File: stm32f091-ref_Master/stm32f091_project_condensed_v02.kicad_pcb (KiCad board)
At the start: 4 copper layers, 68 parts, among them J1 Conn_02x05_Odd_Even, J2 Conn_01x09_Female, J3 Conn_01x08_Female, J4 Conn_01x02_Female, SW1 SW_Push, SW2 SW_Push, U1 LD1117S33TR_SOT223, U2 LM324, U3 STM32F091RCTx, U4 LM386

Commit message: new pcb design
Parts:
- moved J1 0.30 mm to (134.1, 87.9)
- moved R21 0.23 mm to (127.0, 109.2)
- moved J2 0.09 mm to (140.8, 122.8)
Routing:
- net GND: track 10.5 -> 164.3 mm, vias 0 -> 20
- net 3.3V: track 73.1 -> 218.0 mm, vias 0 -> 16
- net /PA13: track 94.0 -> 50.2 mm, vias 0 -> 4
- net /PA4: track 0.00 -> 28.8 mm, vias 0 -> 2
- net Net-(C18-Pad1): track 38.3 -> 64.3 mm, vias 0 -> 1
- net PB8: track 38.0 -> 16.7 mm, vias 0 -> 1
- net PB14: track 17.6 -> 33.8 mm, vias 0 -> 1
- net /PB2: track 2.30 -> 17.0 mm, vias 0 -> 2
- net /NRST: track 36.7 -> 48.0 mm, vias 0 -> 2
- net 5.5V: track 177.1 -> 186.1 mm
- net /PA14: track 72.3 -> 66.7 mm
- net /PC7: track 25.7 -> 31.0 mm
- net Net-(C18-Pad2): track 47.0 -> 50.3 mm, vias 0 -> 1
- net /PC6: track 30.6 -> 33.8 mm, vias 0 -> 4
- net /U5V: track 0.00 -> 2.54 mm
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- added copper zone on B.Cu, net GND
- added copper zone on F.Cu, net GND

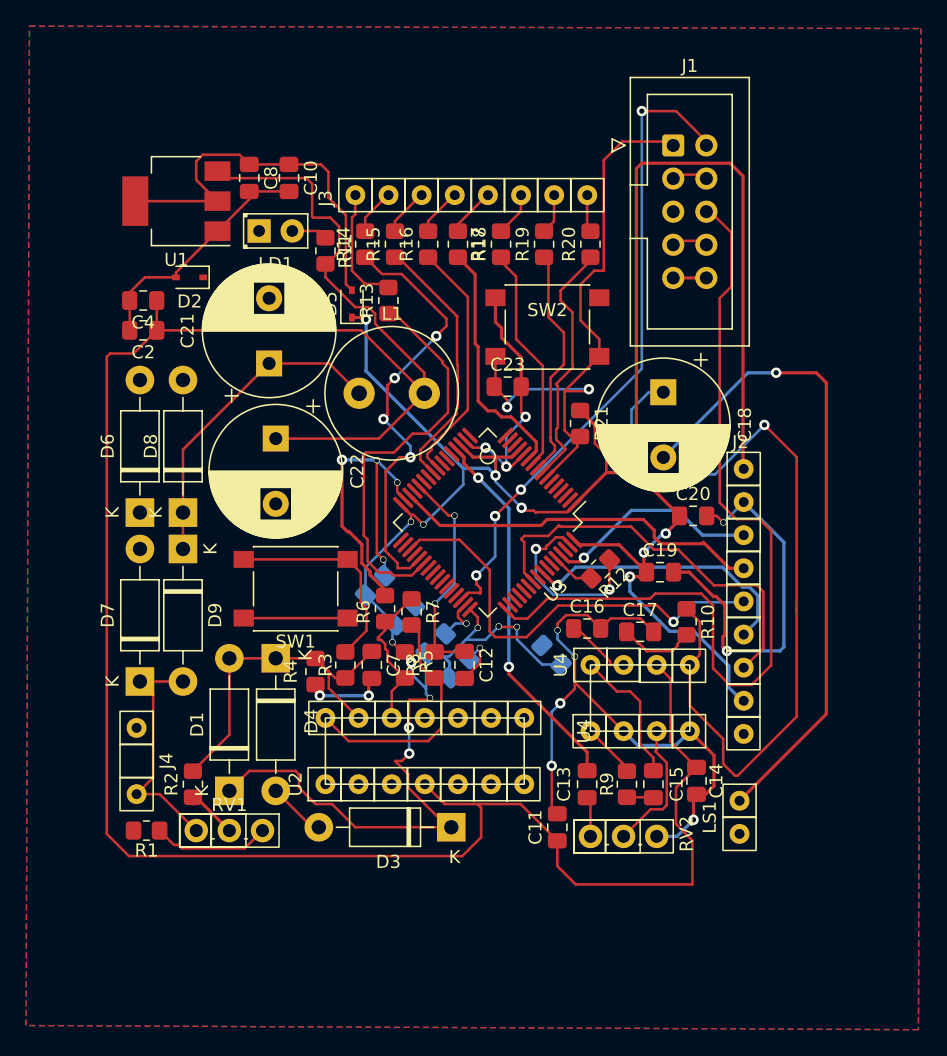
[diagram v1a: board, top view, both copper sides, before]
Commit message: minor tracing changes and edge cut added for v02 pcb
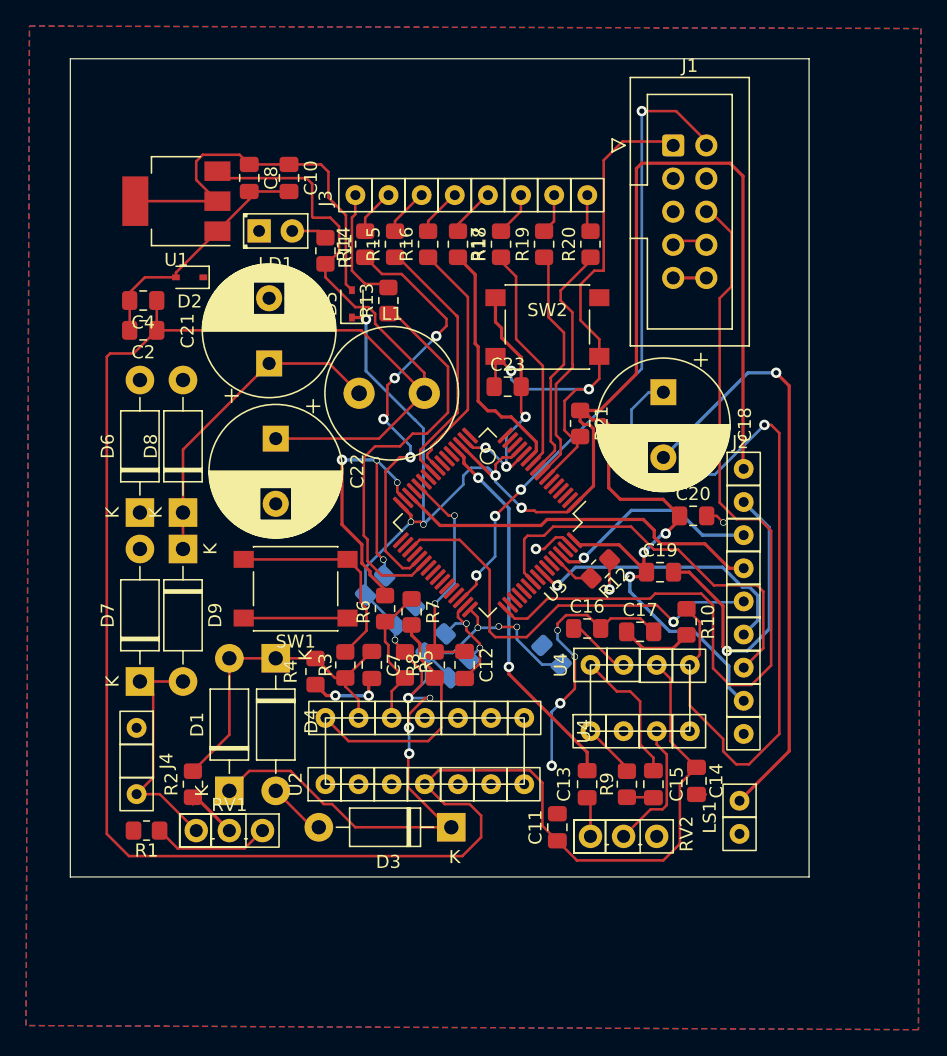
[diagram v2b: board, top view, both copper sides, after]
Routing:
- net GND: track 164.3 -> 124.8 mm, vias 20 -> 19
- net Net-(C18-Pad2): track 50.3 -> 46.1 mm
- net 3.3V: track 218.0 -> 221.6 mm
- net Net-(C18-Pad1): track 64.3 -> 62.1 mm
- net /NRST: track 48.0 -> 46.6 mm
- net 5.5V: track 186.1 -> 187.2 mm
- net /PA13: track 50.2 -> 49.2 mm
- net Net-(C7-Pad1): track 28.1 -> 27.1 mm
- net Net-(R5-Pad2): track 11.8 -> 11.2 mm
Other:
- board outline added: 56.6 x 62.7 mm

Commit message: rick's changes, still need to swap out ic footprints
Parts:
- U4: footprint local_models:U4 -> Package_DIP:DIP-8_W7.62mm
- moved C6 20.5 mm to (119.1, 107.5), turned to 135 degrees
- moved C3 16.4 mm to (127.9, 115.9)
- moved C9 9.84 mm to (123.7, 117.1), turned to 0 degrees
- moved U4 6.02 mm to (128.2, 135.2)
- moved C13 1.97 mm to (128.0, 138.7)
- moved C15 1.92 mm to (133.0, 138.7)
- moved R9 1.91 mm to (130.7, 138.7)
- moved C14 1.90 mm to (135.9, 138.5)
- moved RV2 1.14 mm to (127.8, 142.0)
- moved C1 0.46 mm to (110.9, 121.8)
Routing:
- net GND: track 124.8 -> 135.6 mm, vias 19 -> 20
- net 5.5V: track 187.2 -> 196.8 mm
- net 3.3V: track 221.6 -> 218.0 mm, vias 16 -> 15
- net /PA4: track 28.8 -> 30.9 mm
- net Net-(C7-Pad1): track 27.1 -> 25.7 mm
- net Net-(C15-Pad2): track 10.7 -> 12.1 mm
- net Net-(R2-Pad1): track 5.14 -> 3.85 mm
- net Net-(C18-Pad1): track 62.1 -> 61.0 mm
- net Net-(RV2-Pad2): track 11.1 -> 10.0 mm
- net /PC2: track 18.0 -> 17.1 mm
- net Net-(D3-Pad2): track 5.22 -> 4.46 mm
- net Net-(C13-Pad2): track 3.07 -> 2.31 mm
- net /PB1: track 0.66 -> 0.00 mm
- net /PB0: track 0.66 -> 0.00 mm
- net Net-(R1-Pad1): track 9.65 -> 9.02 mm
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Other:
- copper layers 4 -> 2
- rule pad_to_mask_clearance: 0.05 -> 0
